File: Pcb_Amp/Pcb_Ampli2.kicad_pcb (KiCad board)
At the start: 4 copper layers, 83.1 x 55.7 mm, 56 parts, among them J1 Conn_01x02, J2 Jack-DC, J3 Jack-DC, J5 Conn_01x03, SW1 SW_SPDT

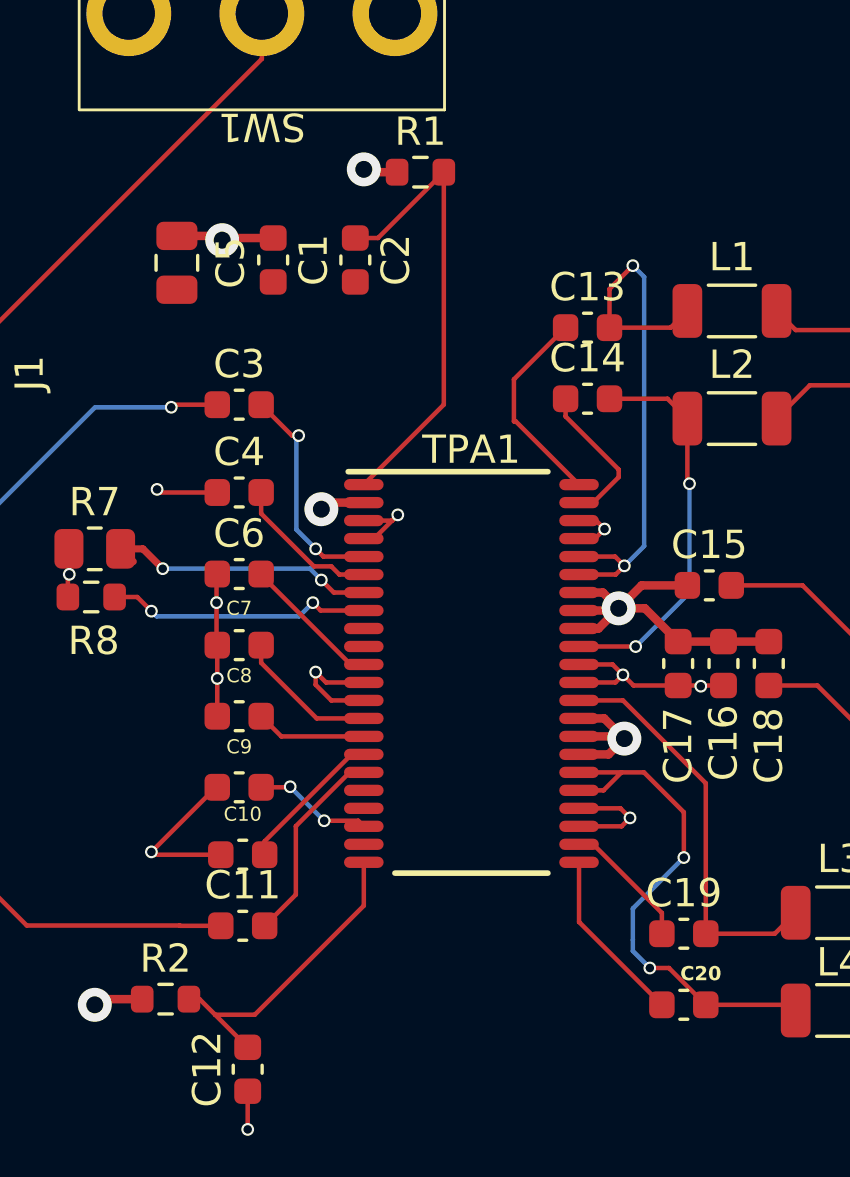
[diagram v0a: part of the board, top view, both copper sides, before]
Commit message: PCBV5_Changes_on_TPA3255
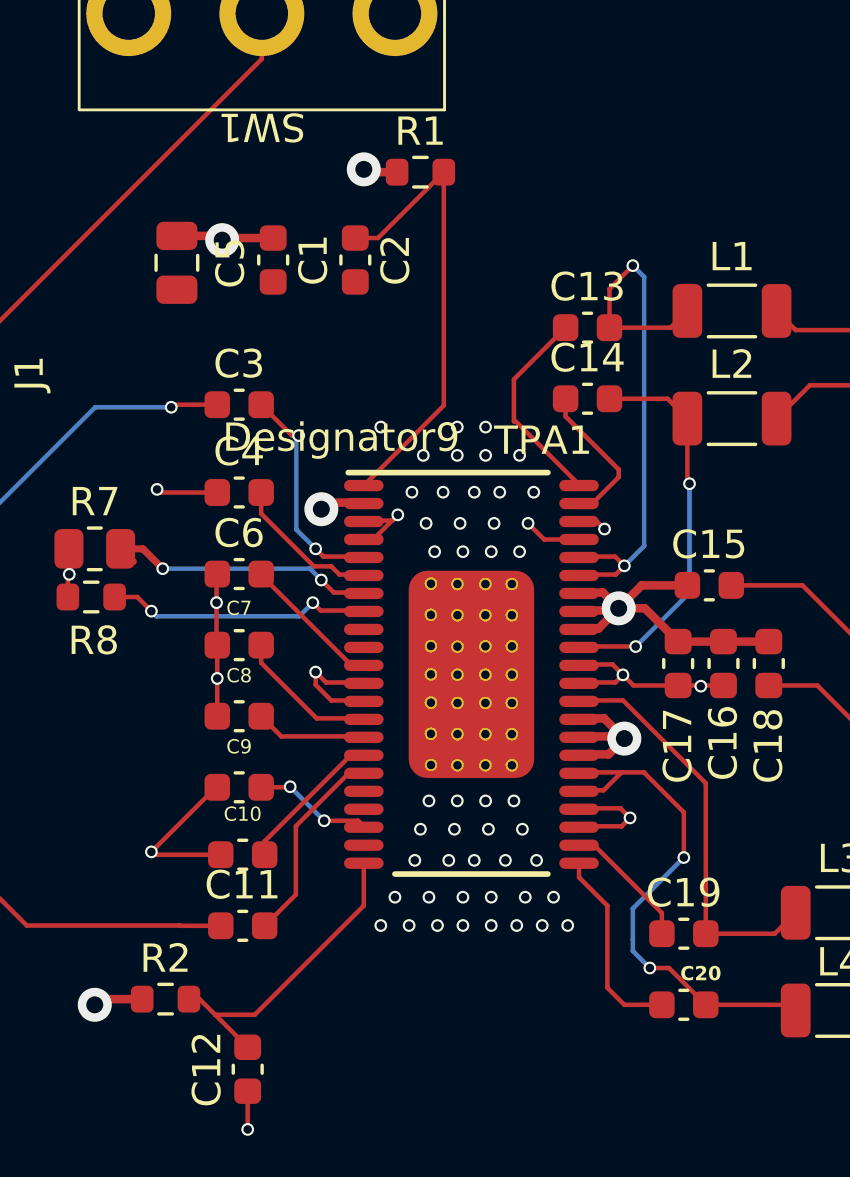
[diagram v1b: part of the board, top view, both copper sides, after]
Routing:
- net GND: track 57.2 -> 58.7 mm, vias 17 -> 64
- net Net-(TPA1-23_BST_D): track 6.24 -> 6.99 mm
